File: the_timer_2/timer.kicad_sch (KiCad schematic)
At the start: 20 parts, among them U1 ESP32-C3FH4, U10 TPS61033DRLR, U2 W25Q128JVS, X2 XRCGB40M000F1S2GR0

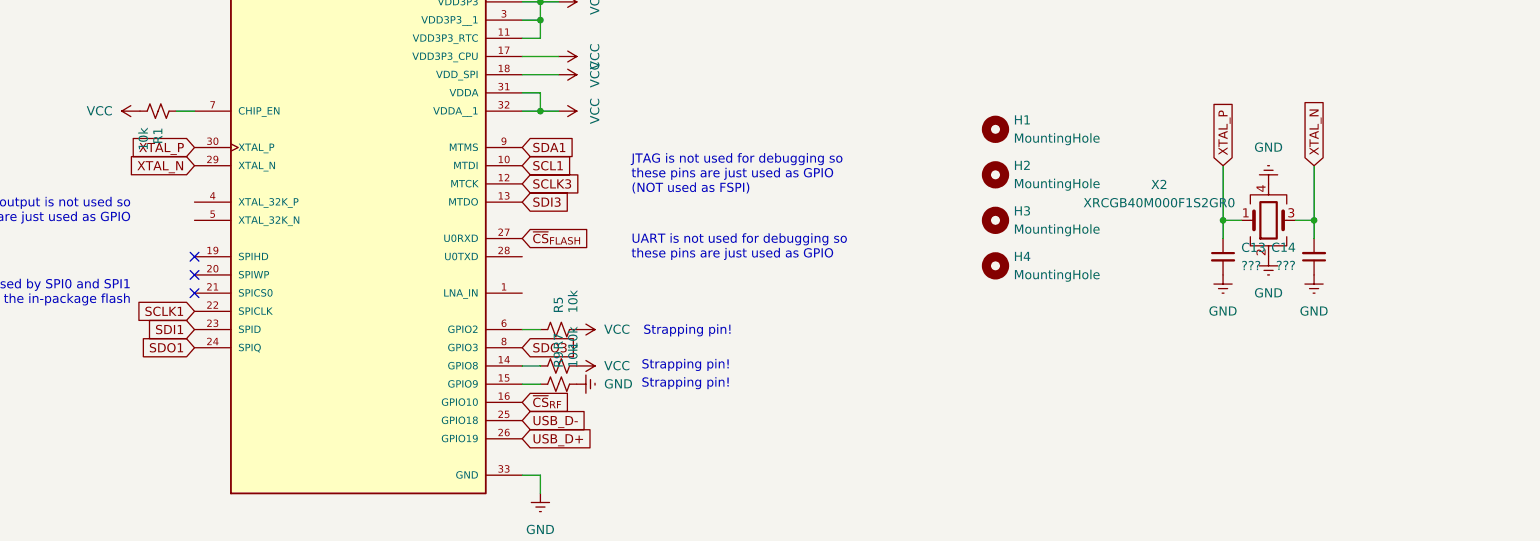
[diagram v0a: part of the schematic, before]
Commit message: Mostly de-exploded the schematic
Also like sorta fixed the PCB design but not really but sorta
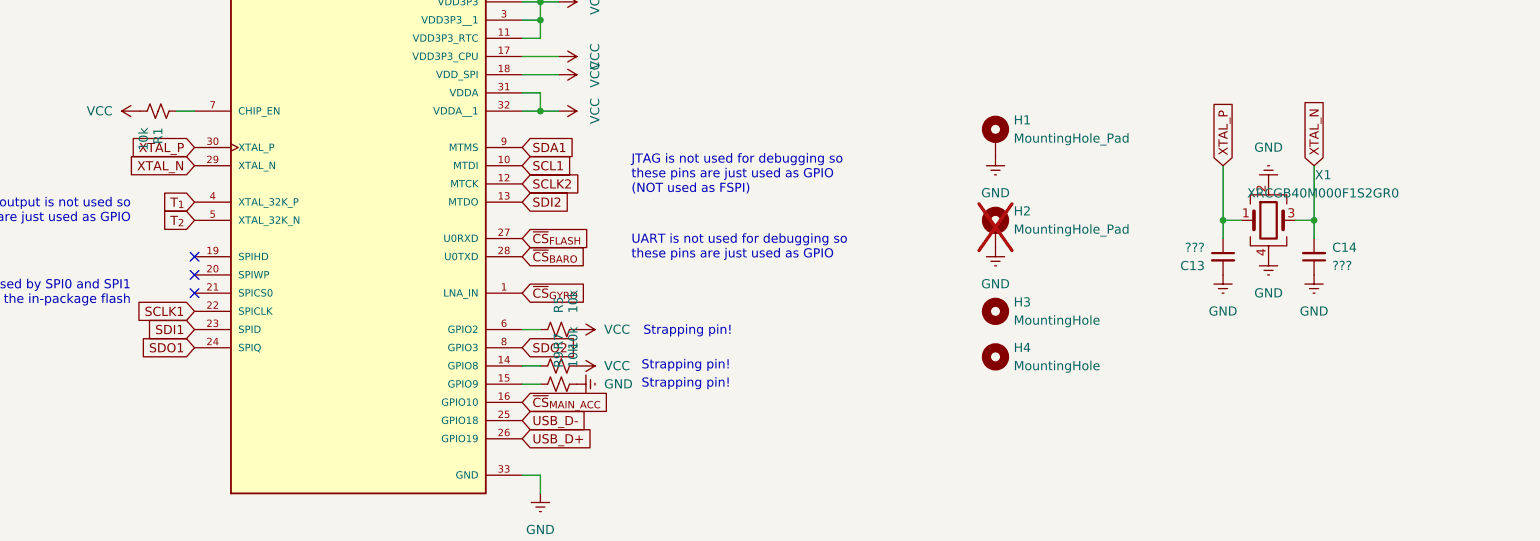
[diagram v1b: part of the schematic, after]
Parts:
- removed H1, H2: MountingHole, MountingHole:MountingHole_3.2mm_M3, symbol Mechanical:MountingHole
- removed X2: XRCGB40M000F1S2GR0, Crystal:Crystal_SMD_2016-4Pin_2.0x1.6mm, symbol Device:Crystal_GND24
- added H1, H2: MountingHole_Pad, MountingHole:MountingHole_3.2mm_M3_Pad, symbol Mechanical:MountingHole_Pad
- added X1: XRCGB40M000F1S2GR0, Crystal:Crystal_SMD_2016-4Pin_2.0x1.6mm, symbol Device:Crystal_GND24
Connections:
- net GND: now also H1.1, H2.1, X1.2, X1.4
- net XTAL_N: now also X1.3
- net XTAL_P: now also X1.1
- net ~{CS}_{GYRO}: now reaches U1.1 (LNA_IN)
- net ~{CS}_{BARO}: now reaches U1.28 (U0TXD)
- net T_{1}: now reaches U1.4 (XTAL_32K_P)
- net T_{2}: now reaches U1.5 (XTAL_32K_N)
- net SCLK3 renamed SCLK2
- net SDI3 renamed SDI2
- net SDO3 renamed SDO2
- net ~{CS}_{RF} renamed ~{CS}_{MAIN_ACC}
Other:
- moved on the sheet: H3, H4
